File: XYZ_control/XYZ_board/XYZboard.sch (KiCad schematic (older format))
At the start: 85 parts, among them J1 DB9_connector, J10 Control_1, J11 Sensor_1, J12 Settings_2, J13 Control_2, J14 Sensor_2, J15 Settings_3, J16 Control_3, J17 Sensor_3, J2 DB9_connector, J3 DB9_connector, J4 PWR IN, J5 Settings_1, U1 A4988_stepper_driver, U2 A4988_stepper_driver, U3 A4988_stepper_driver, U4 LM317MSTT3G_Voltage_Regulator

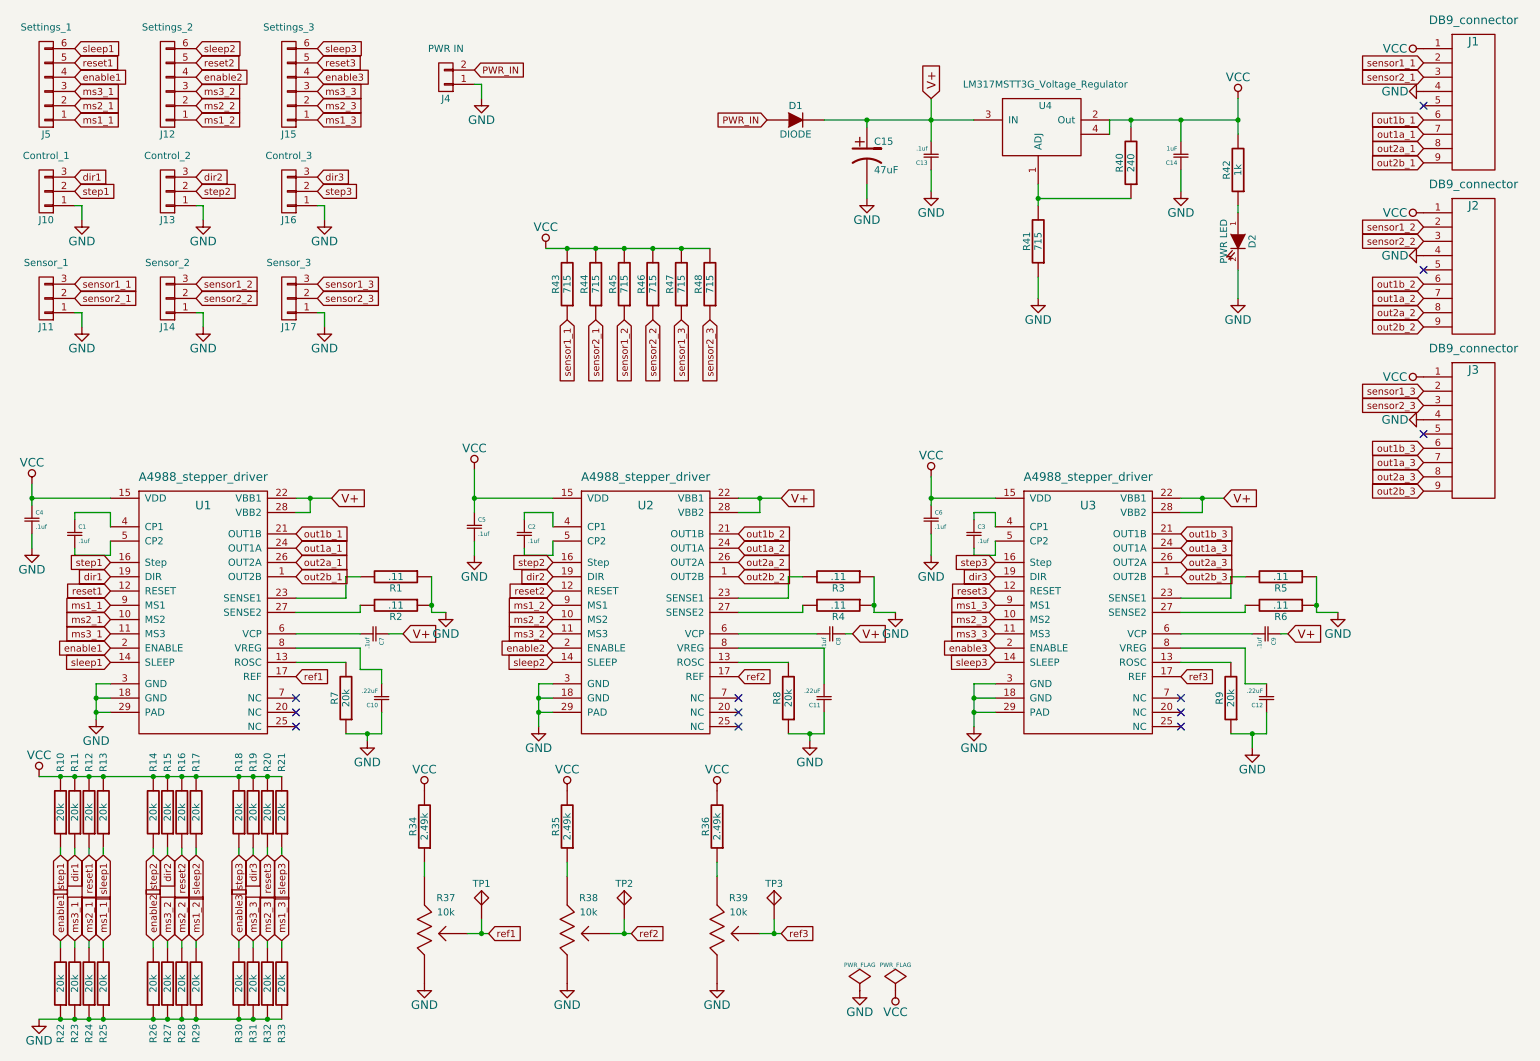
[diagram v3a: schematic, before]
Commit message: Adjusted pinout to processor
rearranged pinout for pins to processor. Removed individual grounds for
each set. Added vcc and gnd out
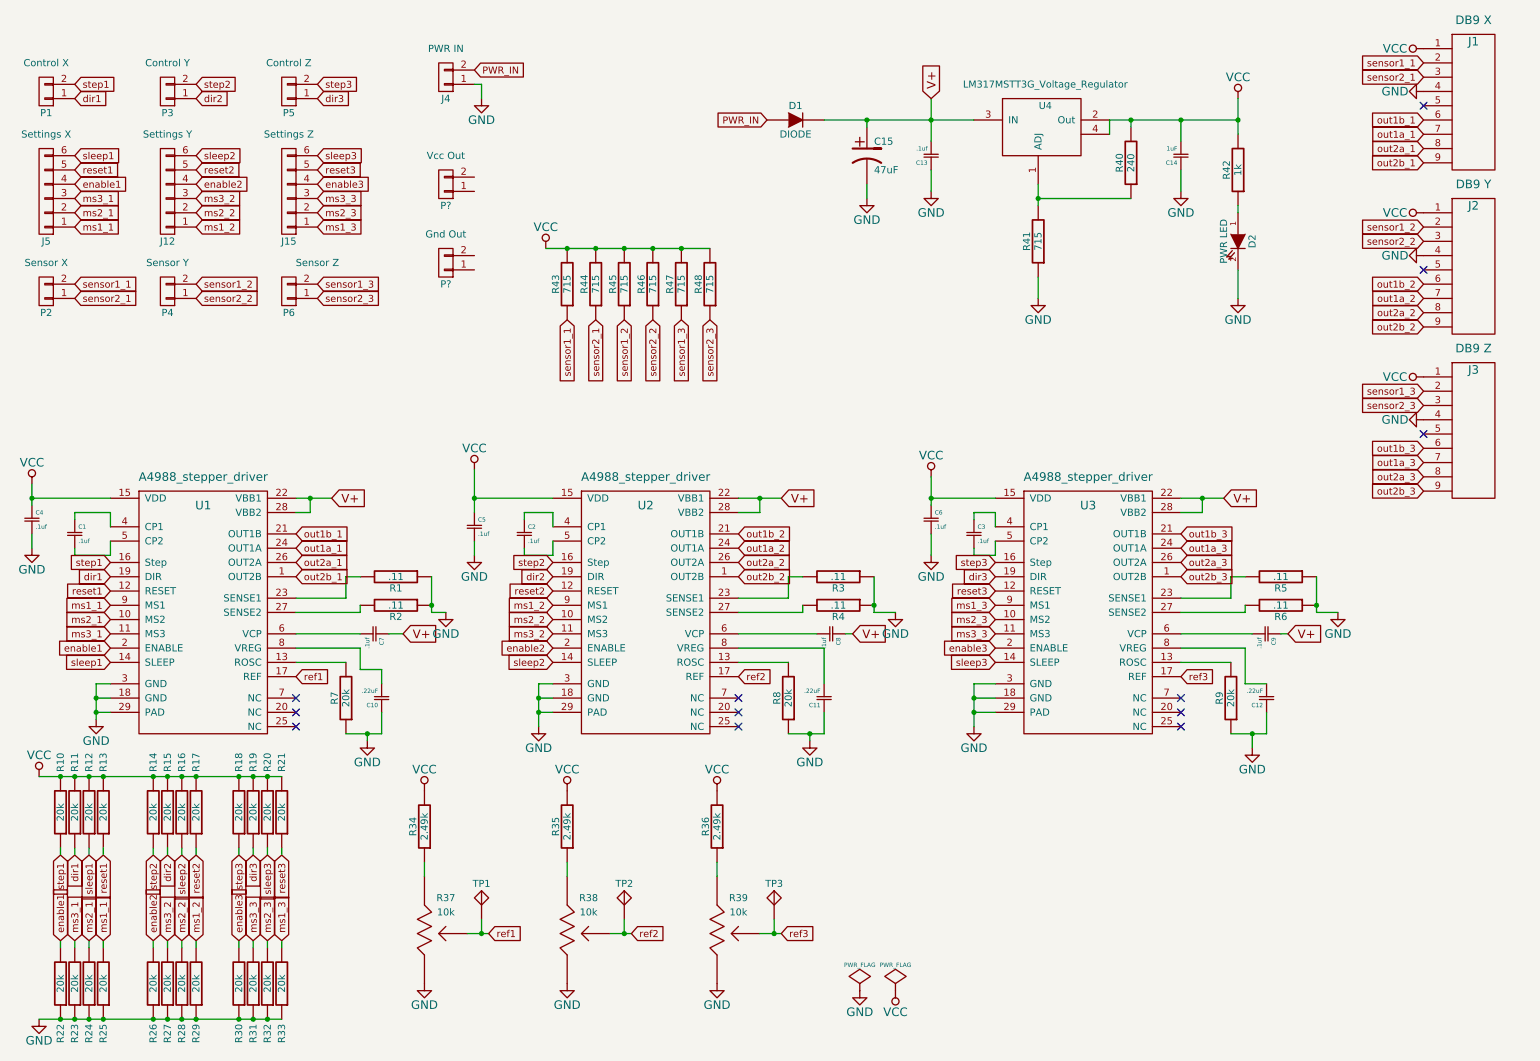
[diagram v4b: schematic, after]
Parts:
- removed J10: Control_1, Pin_Headers:Pin_Header_Straight_1x03, symbol CONN_01X03
- removed J11: Sensor_1, Pin_Headers:Pin_Header_Straight_1x03, symbol CONN_01X03
- removed J13: Control_2, Pin_Headers:Pin_Header_Straight_1x03, symbol CONN_01X03
- removed J14: Sensor_2, Pin_Headers:Pin_Header_Straight_1x03, symbol CONN_01X03
- removed J16: Control_3, Pin_Headers:Pin_Header_Straight_1x03, symbol CONN_01X03
- removed J17: Sensor_3, Pin_Headers:Pin_Header_Straight_1x03, symbol CONN_01X03
- added P1: Control X, symbol CONN_01X02
- added P2: Sensor X, symbol CONN_01X02
- added P3: Control Y, symbol CONN_01X02
- added P4: Sensor Y, symbol CONN_01X02
- added P5: Control Z, symbol CONN_01X02
- added P6: Sensor Z, symbol CONN_01X02
- added P?: Vcc Out, symbol CONN_01X02
- added P?: Gnd Out, symbol CONN_01X02
- J1: value DB9_connector -> DB9 X
- J12: value Settings_2 -> Settings Y
- J15: value Settings_3 -> Settings Z
- J2: value DB9_connector -> DB9 Y
- J3: value DB9_connector -> DB9 Z
- J5: value Settings_1 -> Settings X
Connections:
- net dir1: now also P1.1 (P1)
- net dir2: now also P3.1 (P1)
- net dir3: now also P5.1 (P1)
- net reset1: now also R13.1; no longer R12.1
- net reset2: now also R17.1; no longer R16.1
- net reset3: now also R21.1; no longer R20.1
- net sensor1_1: now also P2.2 (P2)
- net sensor1_2: now also P4.2 (P2)
- net sensor1_3: now also P6.2 (P2)
- net sensor2_1: now also P2.1 (P1)
- net sensor2_2: now also P4.1 (P1)
- net sensor2_3: now also P6.1 (P1)
- net sleep1: now also R12.1; no longer R13.1
- net sleep2: now also R16.1; no longer R17.1
- net sleep3: now also R20.1; no longer R21.1
- net step1: now also P1.2 (P2)
- net step2: now also P3.2 (P2)
- net step3: now also P5.2 (P2)
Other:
- moved on the sheet: J12, J15, J5

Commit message: Replaced pull-up and pull-down
Replaced 20k pull up and pull down resistors with resistor arrays. Also
reannotated the board and updated the BOM
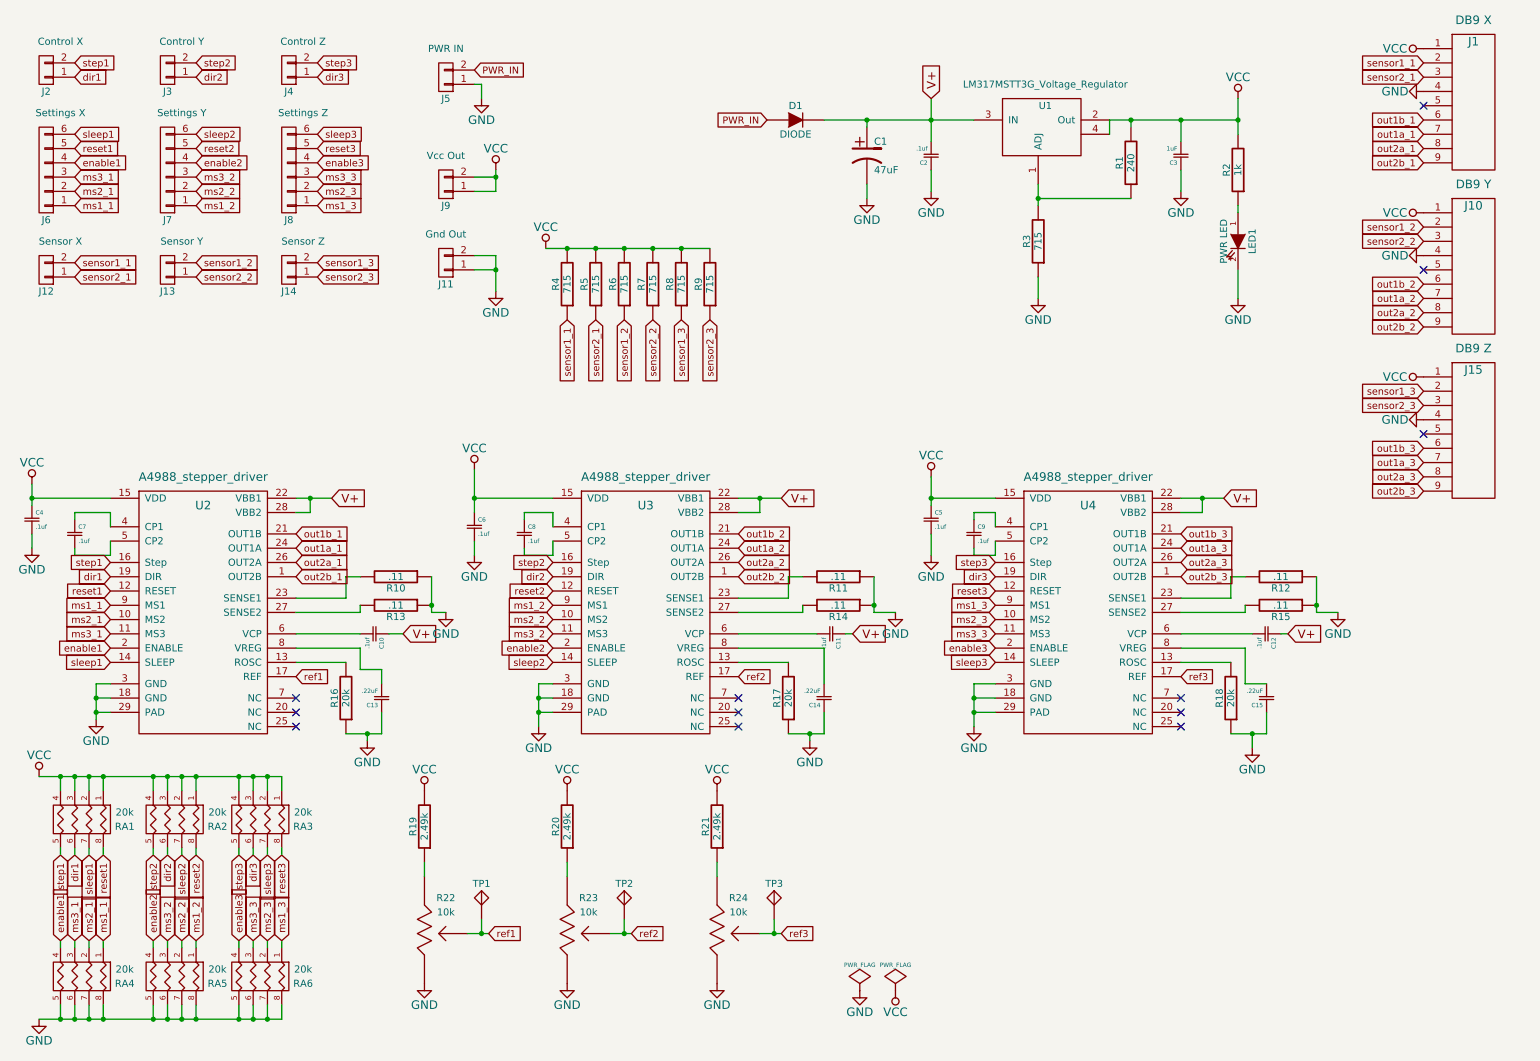
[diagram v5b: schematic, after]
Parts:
- removed R10, R11, R12, R13, R14, R15, R16, R17, R18, R19, R20, R21, R22, R23, R24, R25, R26, R27, R28, R29, R30, R31, R32, R33: 20k, symbol R
- added RA1, RA2, RA3, RA4, RA5, RA6: 20k, symbol R_PACK4
- gave numbers to parts that had none: 2
- renumbered C15 to C1, C7 to C10, C8 to C11, C9 to C12, C10 to C13, C11 to C14, C12 to C15, C13 to C2, C14 to C3, C6 to C5, C5 to C6, C1 to C7, C2 to C8, C3 to C9, J2 to J10, P2 to J12, P4 to J13, P6 to J14, J3 to J15, P1 to J2, P3 to J3, P5 to J4, J4 to J5, J5 to J6, J12 to J7, J15 to J8, D2 to LED1, R40 to R1, R1 to R10, R3 to R11, R5 to R12, R2 to R13, R4 to R14, R6 to R15, R7 to R16, R8 to R17, R9 to R18, R34 to R19, R42 to R2, R35 to R20, R36 to R21, R37 to R22, R38 to R23, R39 to R24, R41 to R3, R43 to R4, R44 to R5, R45 to R6, R46 to R7, R47 to R8, R48 to R9, U4 to U1, U1 to U2, U2 to U3, U3 to U4
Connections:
- net GND: now also J11.1 (P1), J11.2 (P2), RA4.5 (R4), RA4.6 (R3), RA4.7 (R2), RA4.8 (R1), RA5.5 (R4), RA5.6 (R3), RA5.7 (R2), RA5.8 (R1), RA6.5 (R4), RA6.6 (R3), RA6.7 (R2), RA6.8 (R1)
- net VCC: now also J9.1 (P1), J9.2 (P2), RA1.1 (P1), RA1.2 (P2), RA1.3 (P3), RA1.4 (P4), RA2.1 (P1), RA2.2 (P2), RA2.3 (P3), RA2.4 (P4), RA3.1 (P1), RA3.2 (P2), RA3.3 (P3), RA3.4 (P4)
- net dir1: now also RA1.6 (R3)
- net dir2: now also RA2.6 (R3)
- net dir3: now also RA3.6 (R3)
- net enable1: now also RA4.4 (P4)
- net enable2: now also RA5.4 (P4)
- net enable3: now also RA6.4 (P4)
- net ms1_1: now also RA4.1 (P1)
- net ms1_2: now also RA5.1 (P1)
- net ms1_3: now also RA6.1 (P1)
- net ms2_1: now also RA4.2 (P2)
- net ms2_2: now also RA5.2 (P2)
- net ms2_3: now also RA6.2 (P2)
- net ms3_1: now also RA4.3 (P3)
- net ms3_2: now also RA5.3 (P3)
- net ms3_3: now also RA6.3 (P3)
- net reset1: now also RA1.8 (R1)
- net reset2: now also RA2.8 (R1)
- net reset3: now also RA3.8 (R1)
- net sleep1: now also RA1.7 (R2)
- net sleep2: now also RA2.7 (R2)
- net sleep3: now also RA3.7 (R2)
- net step1: now also RA1.5 (R4)
- net step2: now also RA2.5 (R4)
- net step3: now also RA3.5 (R4)
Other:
- moved on the sheet: J12, J13, J14, J2, J3, J4, J6, J7, J8

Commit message: Started board layout
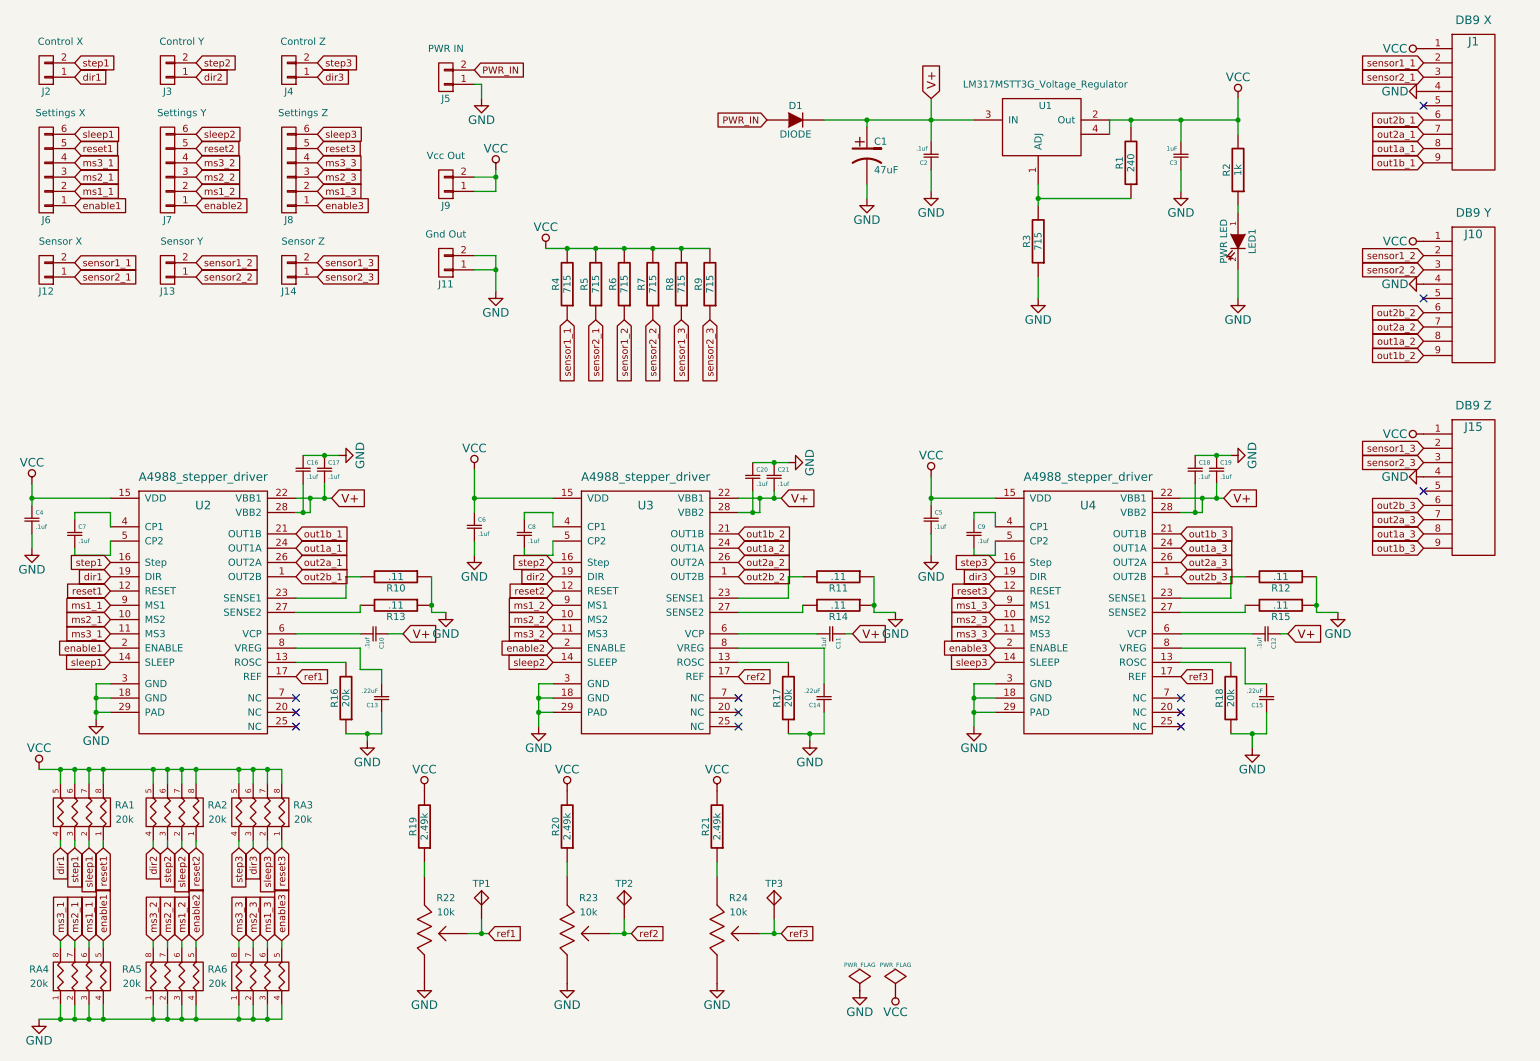
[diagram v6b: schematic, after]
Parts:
- added C16, C17, C18, C19, C20, C21: .1uf, XYZ_footprints:C_0603_HandSoldering, symbol Csmall
- C1: footprint (none) -> XYZ_footprints:PCE3929CT-ND
- C10, C11, C12, C13, C14, C15, C2, C3, C4, C5, C6, C7, C8, C9: footprint (none) -> XYZ_footprints:C_0603_HandSoldering
- D1: footprint (none) -> XYZ_footprints:SD2010S040S3R0
- J1, J10, J15: footprint (none) -> XYZ_footprints:DB9MD
- J11, J12, J13, J14, J2, J3, J4, J9: footprint (none) -> XYZ_footprints:Pin_Header_Straight_1x02
- J5: footprint Pin_Headers:Pin_Header_Straight_1x02 -> XYZ_footprints:Pin_Header_Straight_1x02
- J6, J7, J8: footprint Pin_Headers:Pin_Header_Straight_1x06 -> XYZ_footprints:Pin_Header_Straight_1x06
- LED1: footprint LEDs:LED-0603 -> XYZ_footprints:LGR971-KN-1
- R1, R17, R18, R19, R2, R20, R21, R3: footprint (none) -> XYZ_footprints:R_0603_HandSoldering
- R10, R11, R12, R13, R14, R15: footprint Resistors_SMD:R_0603_HandSoldering -> XYZ_footprints:R_1206_HandSoldering
- R16: footprint Resistors_SMD:R_0402 -> XYZ_footprints:R_0603_HandSoldering
- R22, R23, R24: footprint (none) -> XYZ_footprints:TC33X-103ECT-ND
- R4, R5, R6, R7, R8, R9: footprint Resistors_SMD:R_0603_HandSoldering -> XYZ_footprints:R_0603_HandSoldering
- RA1, RA2, RA3, RA4, RA5, RA6: footprint (none) -> XYZ_footprints:CAT16-203J4LFCT-ND
- U1: footprint SMD_Packages:SOT-223 -> XYZ_footprints:voltage_regulator_sot223
- U2, U3, U4: footprint SMD_Packages:QFN-28-1EP -> XYZ_footprints:Qfn_28_A4988_with_thermal_vias
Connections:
- net GND: now also RA4.1 (P1), RA4.2 (P2), RA4.3 (P3), RA4.4 (P4), RA5.1 (P1), RA5.2 (P2), RA5.3 (P3), RA5.4 (P4), RA6.1 (P1), RA6.2 (P2), RA6.3 (P3), RA6.4 (P4), C16.1, C17.1, C18.1, C19.1, C20.1, C21.1; no longer RA4.5 (R4), RA4.6 (R3), RA4.7 (R2), RA4.8 (R1), RA5.5 (R4), RA5.6 (R3), RA5.7 (R2), RA5.8 (R1), RA6.5 (R4), RA6.6 (R3), RA6.7 (R2), RA6.8 (R1)
- net V+: now also C16.2, C17.2, C18.2, C19.2, C20.2, C21.2
- net VCC: now also RA1.5 (R4), RA1.6 (R3), RA1.7 (R2), RA1.8 (R1), RA2.5 (R4), RA2.6 (R3), RA2.7 (R2), RA2.8 (R1), RA3.5 (R4), RA3.6 (R3), RA3.7 (R2), RA3.8 (R1); no longer RA1.1 (P1), RA1.2 (P2), RA1.3 (P3), RA1.4 (P4), RA2.1 (P1), RA2.2 (P2), RA2.3 (P3), RA2.4 (P4), RA3.1 (P1), RA3.2 (P2), RA3.3 (P3), RA3.4 (P4)
- net dir1: now also RA1.4 (P4); no longer RA1.6 (R3)
- net dir2: now also RA2.4 (P4); no longer RA2.6 (R3)
- net dir3: now also RA3.3 (P3); no longer RA3.6 (R3)
- net enable1: now also J6.1 (P1), RA4.5 (R4); no longer J6.4 (P4), RA4.4 (P4)
- net enable2: now also J7.1 (P1), RA5.5 (R4); no longer J7.4 (P4), RA5.4 (P4)
- net enable3: now also J8.1 (P1), RA6.5 (R4); no longer J8.4 (P4), RA6.4 (P4)
- net ms1_1: now also J6.2 (P2), RA4.6 (R3); no longer J6.1 (P1), RA4.1 (P1)
- net ms1_2: now also J7.2 (P2), RA5.6 (R3); no longer J7.1 (P1), RA5.1 (P1)
- net ms1_3: now also J8.2 (P2), RA6.6 (R3); no longer J8.1 (P1), RA6.1 (P1)
- net ms2_1: now also J6.3 (P3), RA4.7 (R2); no longer J6.2 (P2), RA4.2 (P2)
- net ms2_2: now also J7.3 (P3), RA5.7 (R2); no longer J7.2 (P2), RA5.2 (P2)
- net ms2_3: now also J8.3 (P3), RA6.7 (R2); no longer J8.2 (P2), RA6.2 (P2)
- net ms3_1: now also J6.4 (P4), RA4.8 (R1); no longer J6.3 (P3), RA4.3 (P3)
- net ms3_2: now also J7.4 (P4), RA5.8 (R1); no longer J7.3 (P3), RA5.3 (P3)
- net ms3_3: now also J8.4 (P4), RA6.8 (R1); no longer J8.3 (P3), RA6.3 (P3)
- net out1a_1: now also J1.8; no longer J1.7
- net out1a_2: now also J10.8; no longer J10.7
- net out1a_3: now also J15.8; no longer J15.7
- net out1b_1: now also J1.9; no longer J1.6
- net out1b_2: now also J10.9; no longer J10.6
- net out1b_3: now also J15.9; no longer J15.6
- net out2a_1: now also J1.7; no longer J1.8
- net out2a_2: now also J10.7; no longer J10.8
- net out2a_3: now also J15.7; no longer J15.8
- net out2b_1: now also J1.6; no longer J1.9
- net out2b_2: now also J10.6; no longer J10.9
- net out2b_3: now also J15.6; no longer J15.9
- net reset1: now also RA1.1 (P1); no longer RA1.8 (R1)
- net reset2: now also RA2.1 (P1); no longer RA2.8 (R1)
- net reset3: now also RA3.1 (P1); no longer RA3.8 (R1)
- net sleep1: now also RA1.2 (P2); no longer RA1.7 (R2)
- net sleep2: now also RA2.2 (P2); no longer RA2.7 (R2)
- net sleep3: now also RA3.2 (P2); no longer RA3.7 (R2)
- net step1: now also RA1.3 (P3); no longer RA1.5 (R4)
- net step2: now also RA2.3 (P3); no longer RA2.5 (R4)
- net step3: now also RA3.4 (P4); no longer RA3.5 (R4)
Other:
- moved on the sheet: J10, J15, RA1, RA2, RA3

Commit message: xyz board progress
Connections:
- net dir3: now also RA3.4 (P4); no longer RA3.3 (P3)
- net step3: now also RA3.3 (P3); no longer RA3.4 (P4)
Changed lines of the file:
@@
 Text GLabel 1800 6400 3    49   Input ~ 0
 sleep2
+Text GLabel 2300 6400 3    49   Input ~ 0
+step3
 Text GLabel 2200 6400 3    49   Input ~ 0
-step3
-Text GLabel 2300 6400 3    49   Input ~ 0
 dir3
 Text GLabel 2500 6400 3    49   Input ~ 0
